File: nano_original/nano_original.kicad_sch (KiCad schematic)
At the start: 32 parts, among them J1 USB_B_Micro, J2 Conn_01x15, J3 Conn_01x15, J4 Conn_02x03_Odd_Even, SW1 SW_Push, U1 LM1117MP-5.0, U2 FT231XS, U3 ATmega328P-MUR, Y1 16MHz

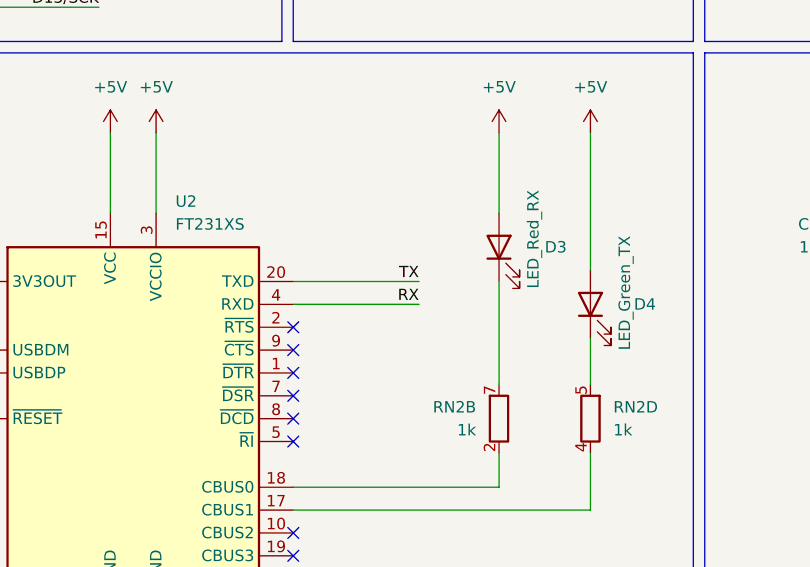
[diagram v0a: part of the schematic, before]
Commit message: critical fix: swap tx and rx between atmega328p and ft231 (smooth brain moment)
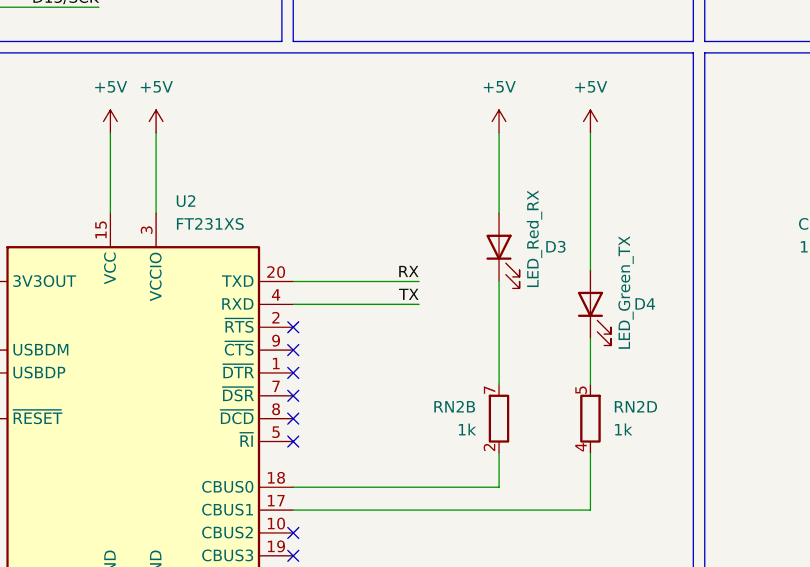
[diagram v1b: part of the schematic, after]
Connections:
- net RX: now also U2.20 (TXD); no longer U2.4 (RXD)
- net TX: now also U2.4 (RXD); no longer U2.20 (TXD)
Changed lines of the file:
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@@
+		)
+	)
+	(label "TX"
+		(at 127 92.71 180)
+		(effects
+			(font
+				(size 1.2446 1.2446)
+			)
+			(justify right bottom)
 		)
 	)
@@
 			)
 			(justify left bottom)
+		)
+	)
+	(label "RX"
+		(at 127 90.17 180)
+		(effects
+			(font
+				(size 1.2446 1.2446)
+			)
+			(justify right bottom)
 		)
 	)
@@
 		)
 	)
-	(label "TX"
-		(at 127 90.17 180)
-		(effects
-			(font
-				(size 1.2446 1.2446)
-			)
-			(justify right bottom)
-		)
-	)
-	(label "RX"
-		(at 127 92.71 180)
-		(effects
-			(font
-				(size 1.2446 1.2446)
-			)
-			(justify right bottom)
-		)
-	)
